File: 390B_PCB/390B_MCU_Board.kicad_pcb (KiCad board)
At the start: 2 copper layers, 13 parts, among them J1 Conn_01x06_Pin, J3 Conn_01x05_Pin

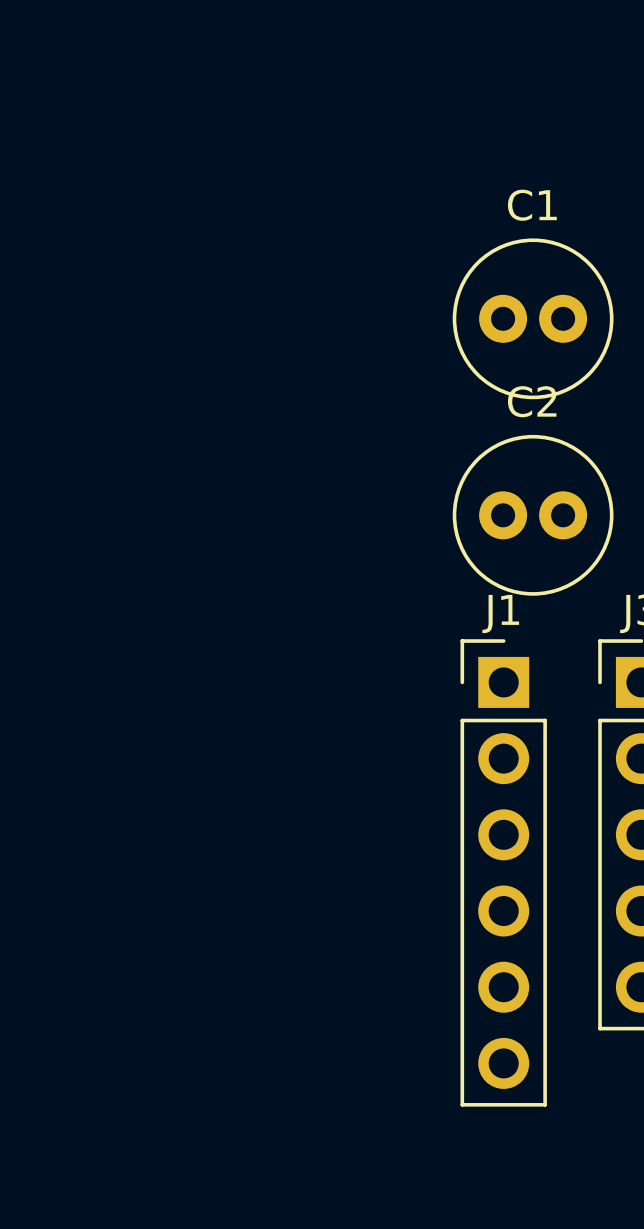
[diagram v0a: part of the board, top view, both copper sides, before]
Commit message: PCB Footprints
All footprints added to pcb now need to clean it up and create copper
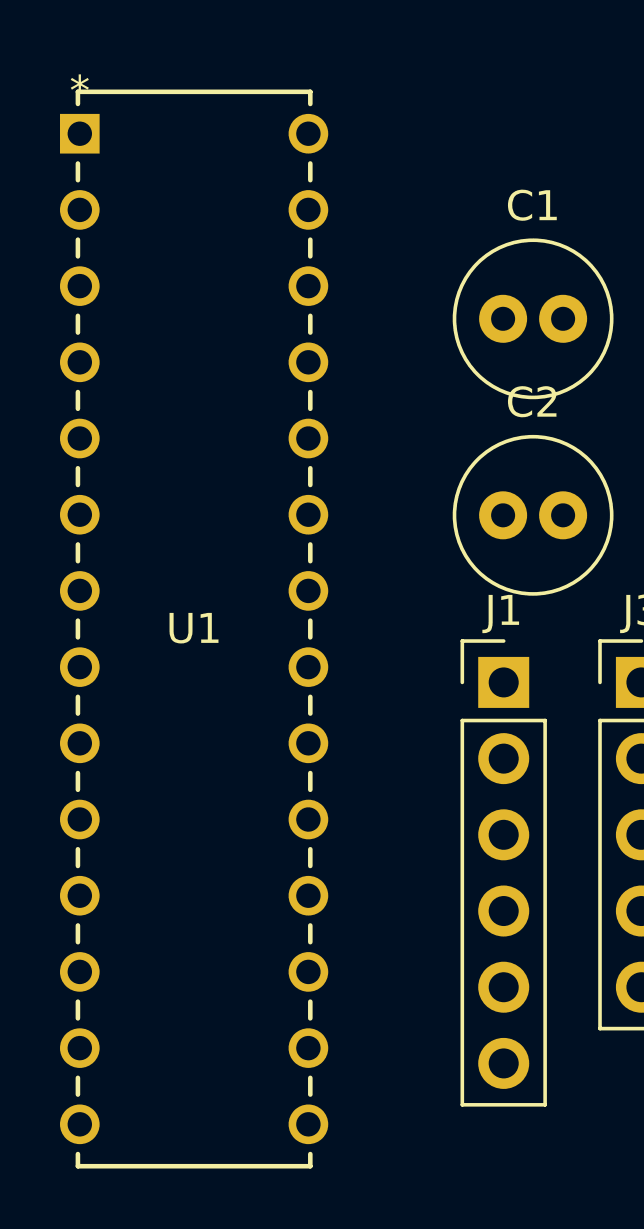
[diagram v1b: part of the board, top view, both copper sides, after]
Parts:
- added U1: ATMEGA328-PU, 390B_Footprint_Library:28P3_SPDIP28_SP_MCH, F.Cu at (111.6, 83.6)

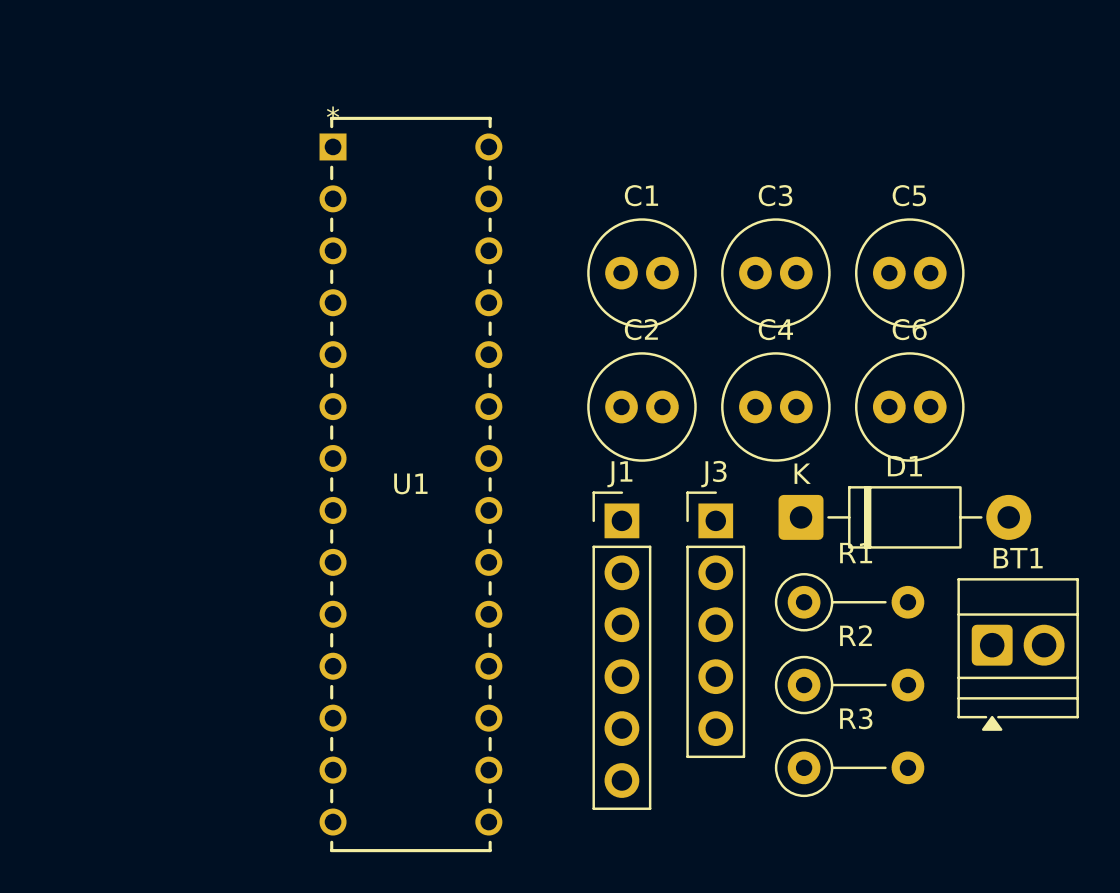
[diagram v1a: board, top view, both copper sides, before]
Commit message: Reorganized PCB Draft 1
Cleaned rats nest, place capacitors close to necessary MCU pins. Need to make sure everything placed optimally.
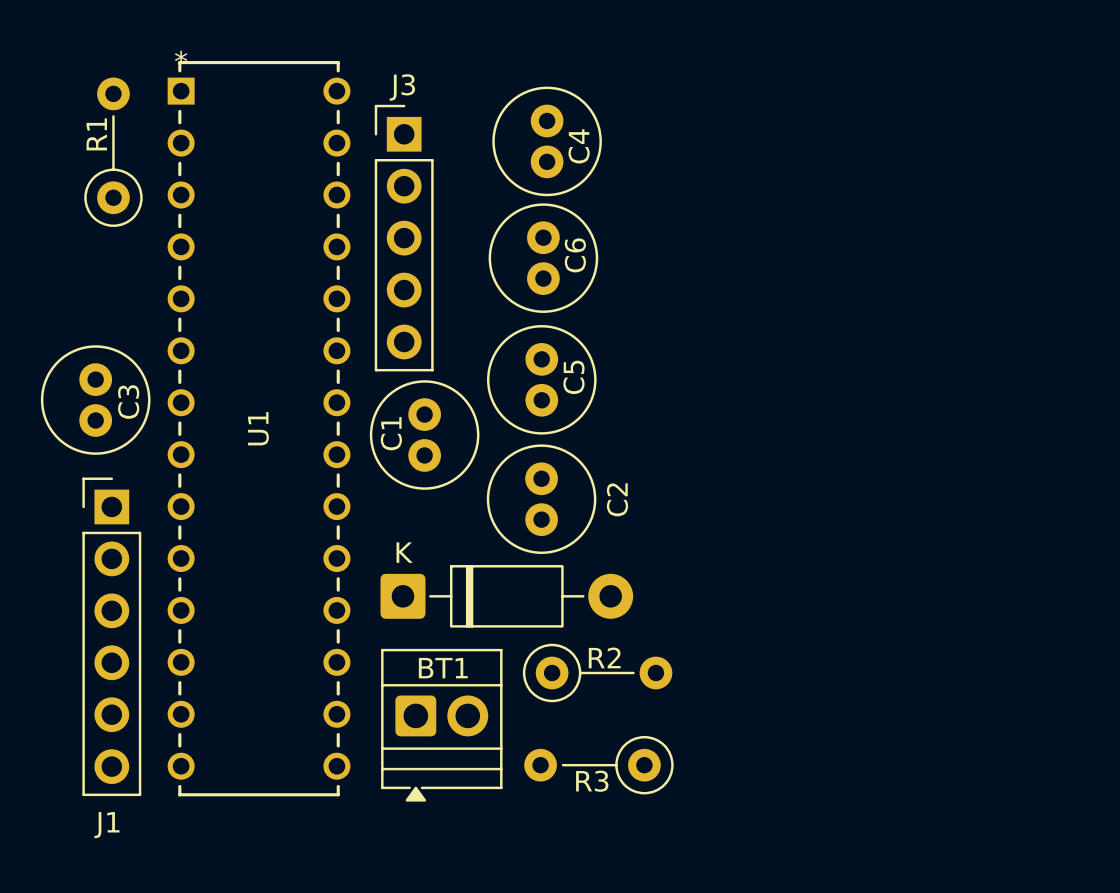
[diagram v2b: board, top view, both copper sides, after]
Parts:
- moved R1 39.1 mm to (100.9, 86.1), turned to 90 degrees
- moved C3 32.7 mm to (100.0, 95.0), turned to -90 degrees
- moved BT1 28.4 mm to (115.7, 111.4)
- moved J1 25.0 mm to (100.8, 101.2)
- moved J3 24.3 mm to (115.1, 83.0)
- moved D1 19.8 mm to (115.0, 105.5)
- moved C6 18.8 mm to (121.9, 88.0), turned to -90 degrees
- moved C5 17.5 mm to (121.8, 94.0), turned to -90 degrees
- moved C4 17.3 mm to (122.1, 82.3), turned to -90 degrees
- moved C1 13.1 mm to (116.1, 98.7), turned to 90 degrees
- moved R2 12.3 mm to (122.3, 109.3)
- moved U1 7.92 mm to (104.2, 80.8)
- moved R3 7.81 mm to (126.8, 113.8), turned to 180 degrees
- moved C2 5.25 mm to (121.8, 99.8), turned to -90 degrees

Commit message: Updated!
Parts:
- added J1: Programmer Connector, Connector_PinHeader_2.54mm:PinHeader_2x03_P2.54mm_Vertical, F.Cu at (142.3, 69.9)
- added U2: ~, 390B_Footprint_Library:Boost, F.Cu at (158.1, 40.0)
- added U3: ~, 390B_Footprint_Library:Charger, F.Cu at (194.2, 36.1)
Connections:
- net Net-(U1-PC6(PCINT14/RESET)) renamed /RESET
- U1 pad 13: unconnected-(U1-PD7(PCINT23/AIN1)-Pad13) -> /charge en
- U1 pad 14: unconnected-(U1-PB0(PCINT0/CLKO/ICP1)-Pad14) -> /boost en
- U1 pad 15: /Motor 2 -> /Motor 1
- U1 pad 16: /Motor 1 -> /Motor 2
- U1 pad 17: /change en -> /MOSI
- U1 pad 18: /boost en -> /MISO
- U1 pad 19: unconnected-(U1-PB5(SCK/PCINT5)-Pad19) -> /SCK

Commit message: Update
Fixed some footprint errors need to make sure everything fixed though before layout
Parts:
- added J3: Screw_Terminal_01x06, TerminalBlock:TerminalBlock_MaiXu_MX126-5.0-06P_1x06_P5.00mm, F.Cu at (125.4, 132.1)
- added J4: Screw_Terminal_01x06, TerminalBlock:TerminalBlock_MaiXu_MX126-5.0-06P_1x06_P5.00mm, F.Cu at (125.4, 142.2)
- added R4: 10k, Resistor_THT:R_Axial_DIN0207_L6.3mm_D2.5mm_P5.08mm_Vertical, F.Cu at (186.4, 102.7)
- added R5: 10k, Resistor_THT:R_Axial_DIN0207_L6.3mm_D2.5mm_P5.08mm_Vertical, F.Cu at (186.4, 106.7)
- added R6: 10k, Resistor_THT:R_Axial_DIN0207_L6.3mm_D2.5mm_P5.08mm_Vertical, F.Cu at (186.4, 110.8)
- added R7: 10k, Resistor_THT:R_Axial_DIN0207_L6.3mm_D2.5mm_P5.08mm_Vertical, F.Cu at (186.4, 114.8)
- moved J3 38.7 mm to (134.1, 81.5), turned to 180 degrees
- moved R1 36.1 mm to (96.0, 50.3), turned to 0 degrees
- moved J4 31.3 mm to (123.4, 52.8)
- moved C1 31.1 mm to (116.8, 67.5)
- moved U1 30.5 mm to (104.2, 50.3)
- moved C4 29.0 mm to (147.3, 96.5)
- moved C3 29.0 mm to (97.5, 66.1)
- moved C5 22.4 mm to (116.8, 72.1)
- moved D1 15.3 mm to (100.1, 102.1), turned to 180 degrees
- moved J1 13.2 mm to (146.8, 82.3)
- moved BT1 13.0 mm to (102.6, 111.3)
- moved R2 8.17 mm to (114.3, 107.7)
- moved U2 3.69 mm to (158.2, 43.7)
- moved U3 3.62 mm to (197.9, 36.1)
- moved C6 3.23 mm to (118.9, 86.9)
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- renumbered J1 to J3, J3 to J4
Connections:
- R2 pad 1: /V_Battery -> GND
- U1 pad 2: /program RX -> unconnected-(U1-PDO(PCINT16/RXD)-Pad2)
- U1 pad 28: /batt temp read -> unconnected-(U1-PC5(ADC5/SCL/PCINT13)-Pad28)
- U1 pad 3: /program TX -> unconnected-(U1-PD1(PCINT17/TXD)-Pad3)
- U2 pad 1: unconnected-(U2-Bat-Pad1) -> GND
- U2 pad 2: unconnected-(U2-GND-Pad2) -> GND
- U2 pad 3: unconnected-(U2-EN-Pad3) -> /VCC
- U2 pad 4: unconnected-(U2-LB-Pad4) -> GND
- U2 pad 6: unconnected-(U2-5V-Pad6) -> /boost en
- U3 pad 11: unconnected-(U3-GND-Pad11) -> GND
- U3 pad 2: unconnected-(U3-GND-Pad2) -> GND
- U3 pad 3: unconnected-(U3-THERM-Pad3) -> GND
- U3 pad 5: unconnected-(U3-CE-Pad5) -> /charge en
- U3 pad 9: unconnected-(U3-GND-Pad9) -> GND

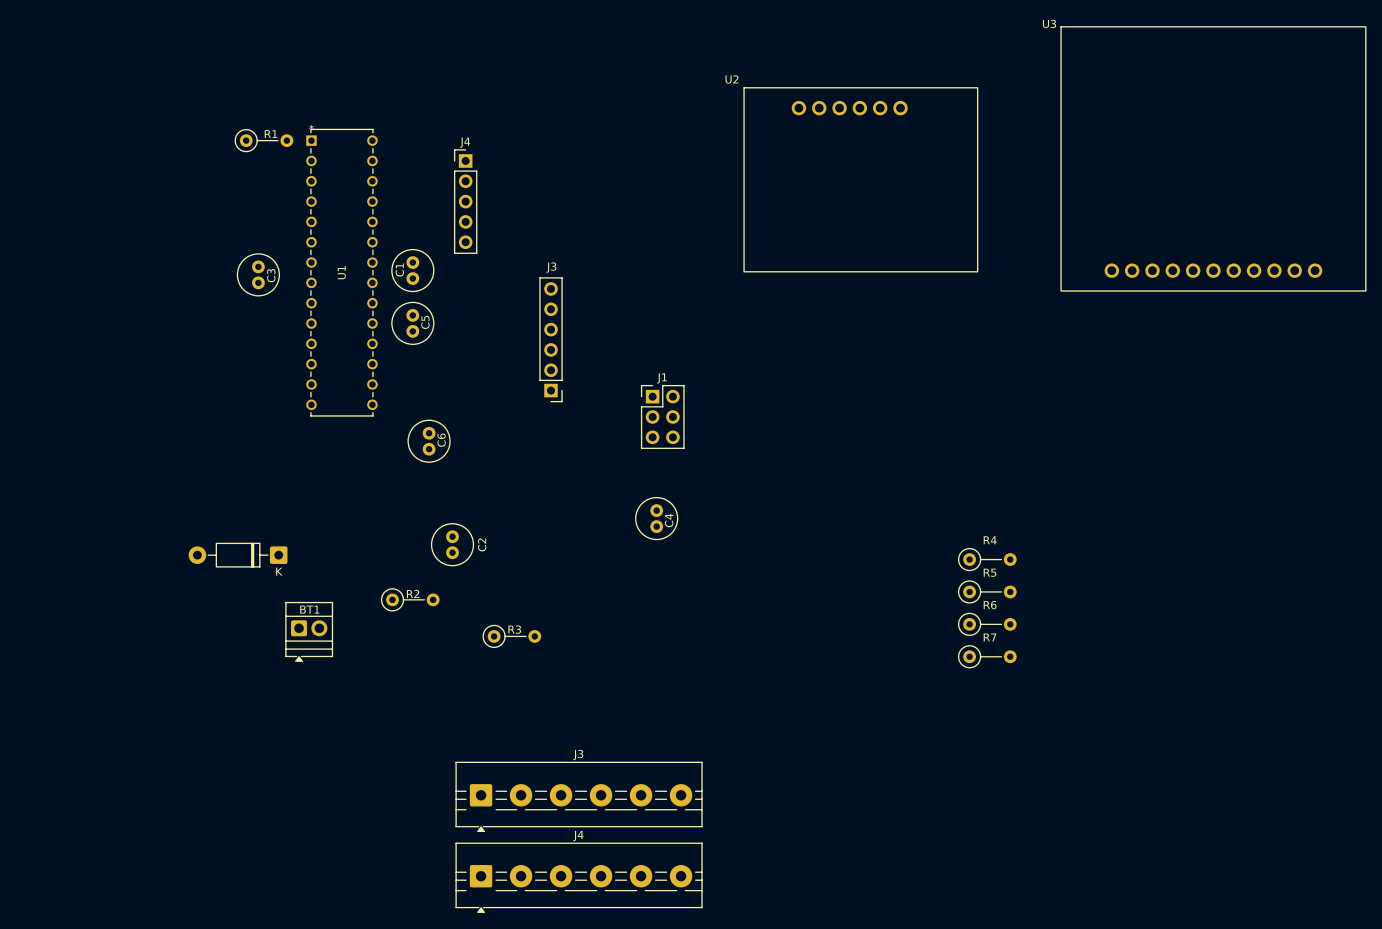
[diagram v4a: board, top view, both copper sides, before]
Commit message: Almost done
PCB corrected and layout complete, just need to add the traces.
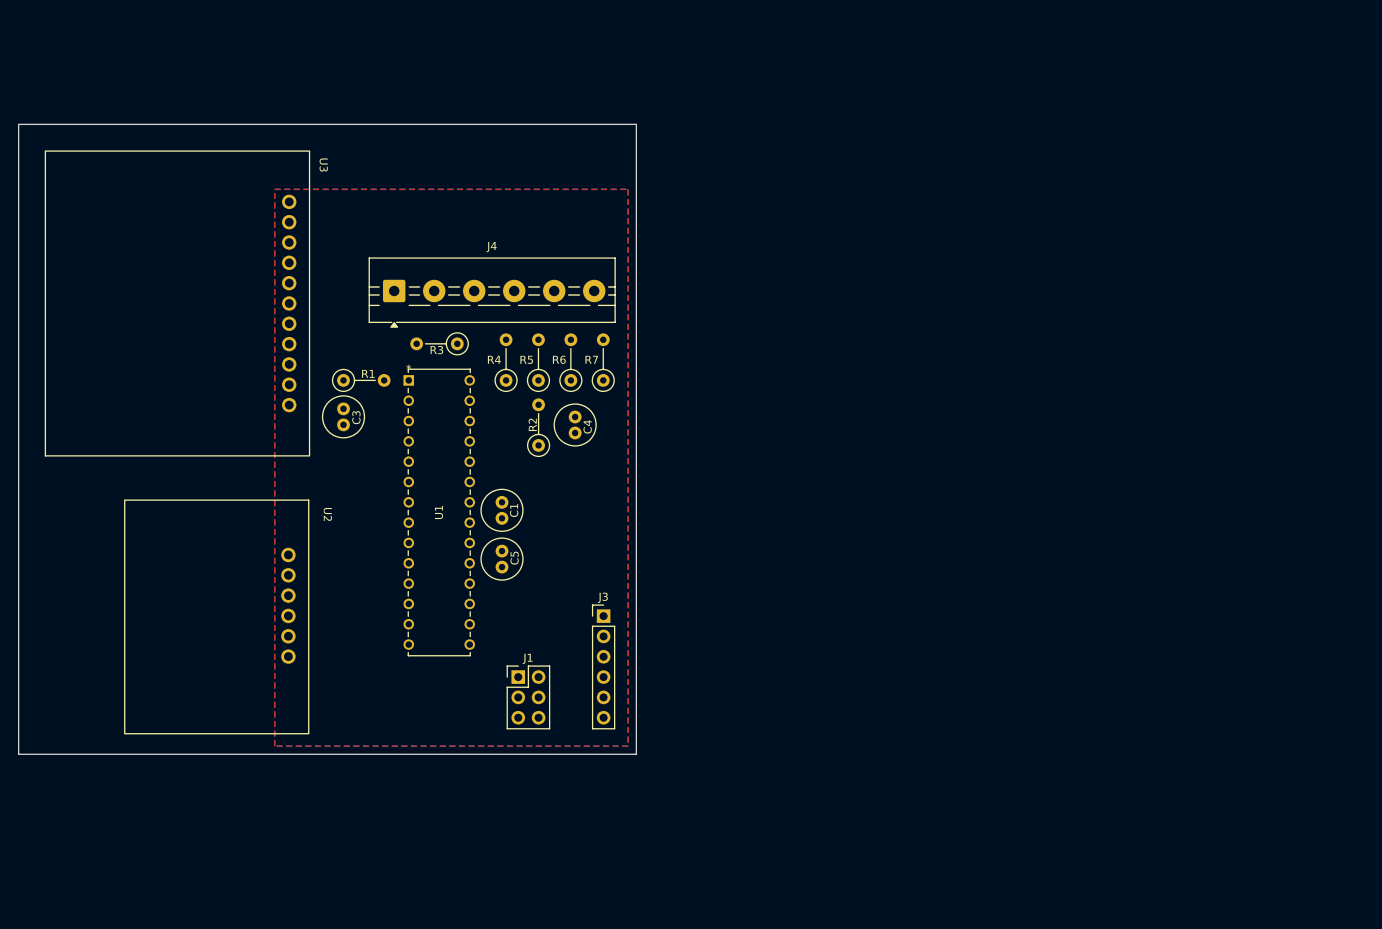
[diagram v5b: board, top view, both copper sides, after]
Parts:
- removed BT1: Sys pin on charging module, TerminalBlock:TerminalBlock_Xinya_XY308-2.54-2P_1x02_P2.54mm_Horizontal
- removed C2, C6: 1000uF, Capacitor_THT:C_Radial_D5.0mm_H11.0mm_P2.00mm
- removed D1: 1N5817, Diode_THT:D_DO-41_SOD81_P10.16mm_Horizontal
- removed the J3 at (134.1, 81.5)
- removed the J3 at (125.4, 132.1)
- removed the J4 at (123.4, 52.8)
- added J3: Motor Pins, Connector_PinHeader_2.54mm:PinHeader_1x06_P2.54mm_Vertical, F.Cu at (140.7, 109.7)
- J4: value Screw_Terminal_01x06 -> Photo R Pins
- moved U3 137.8 mm to (70.9, 89.7), turned to 90 degrees
- moved U2 74.9 mm to (103.8, 95.2), turned to -90 degrees
- moved J4 74.0 mm to (114.5, 69.1)
- moved R4 62.1 mm to (128.5, 80.3), turned to 90 degrees
- moved R5 60.0 mm to (132.5, 80.3), turned to 90 degrees
- moved R6 58.4 mm to (136.6, 80.3), turned to 90 degrees
- moved R7 57.4 mm to (140.6, 80.3), turned to 90 degrees
- moved J1 38.9 mm to (130.0, 117.3)
- moved R3 36.9 mm to (122.4, 75.7), turned to 180 degrees
- moved R1 32.3 mm to (108.2, 80.3)
- moved U1 32.3 mm to (116.3, 80.3)
- moved C1 32.0 mm to (128.0, 97.5)
- moved C5 31.5 mm to (128.0, 101.6)
- moved R2 26.6 mm to (132.6, 88.4), turned to 90 degrees
- moved C3 20.7 mm to (108.2, 83.8)
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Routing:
- added copper zone on F.Cu, net (none)
- added copper zone on B.Cu, net GND
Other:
- board outline added: 77.2 x 78.7 mm
- board text added: "SOLdier V1 Aidan Courduvelis Chase Rubin 390B"

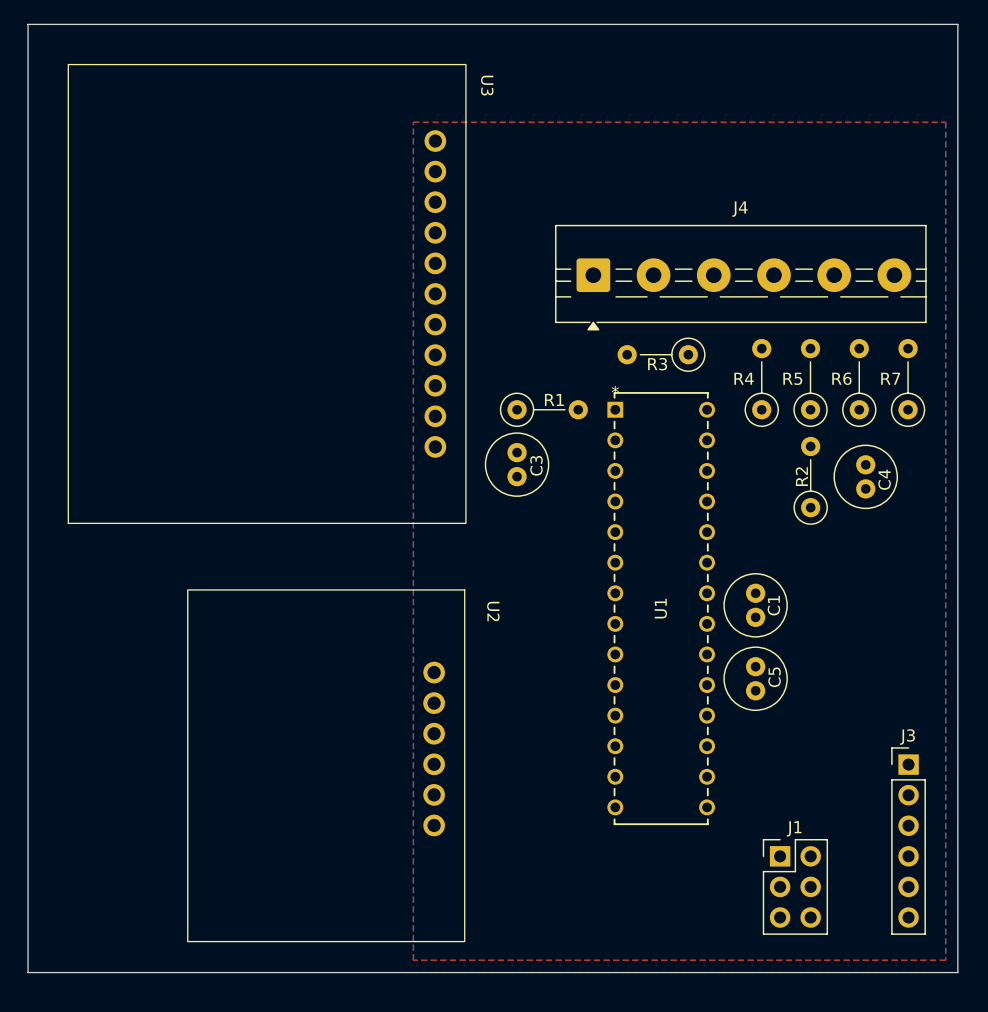
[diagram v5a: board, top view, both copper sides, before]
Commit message: Dimensions
Rounded dimensions for PCB edges
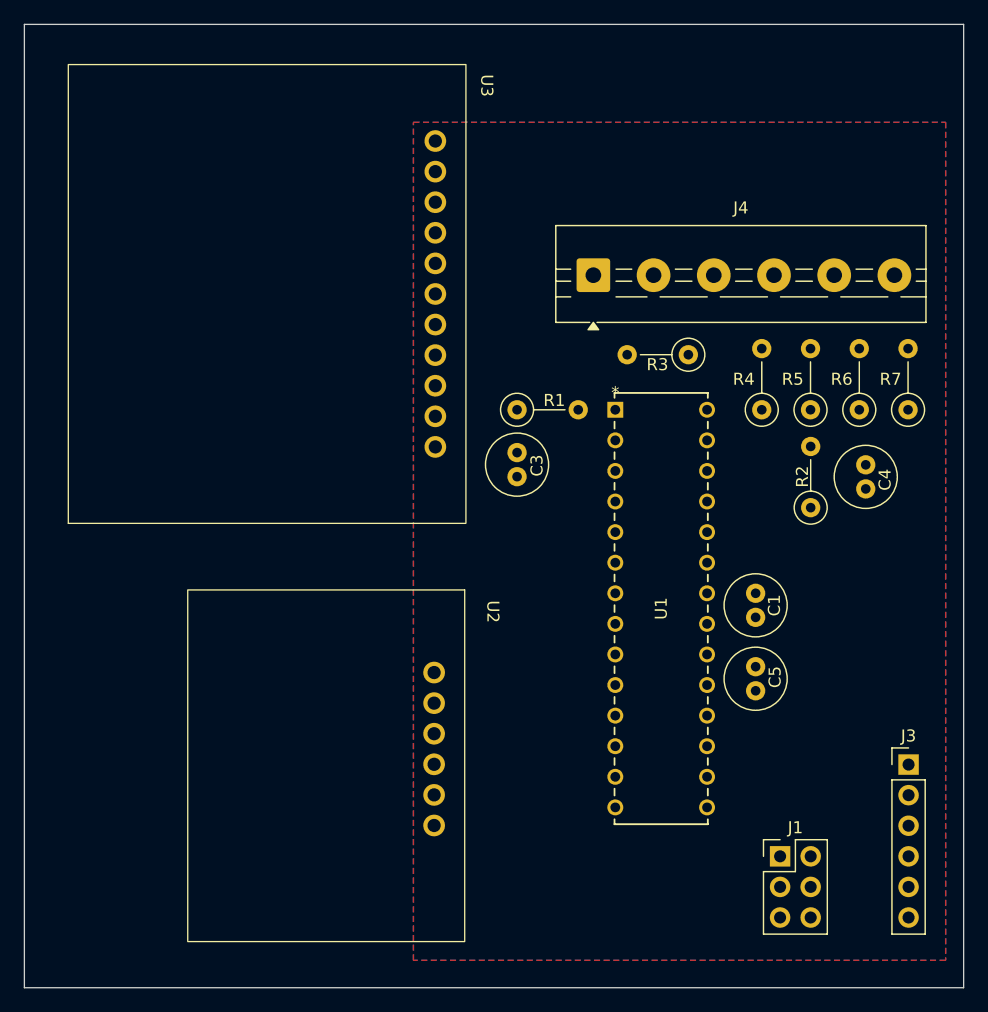
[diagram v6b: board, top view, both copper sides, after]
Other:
- board size 77.2 x 78.7 mm -> 78 x 80 mm
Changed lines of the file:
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@@
 	)
 	(gr_rect
-		(start 67.564 48.26)
-		(end 144.78 127)
+		(start 67.26 48.26)
+		(end 145.26 128.26)
 		(stroke
 			(width 0.05)
-			(type default)
+			(type solid)
 		)
 		(fill no)
